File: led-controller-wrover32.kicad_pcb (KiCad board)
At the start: 4 copper layers, 36 x 40 mm, 130 parts, among them J101 Molex PicoBlade 6-pin, J102 Molex PicoBlade 4-pin, J103 STATUS OUT, J104 USB_B_Micro, J105 POWER IN, J106 Molex PicoBlade 6-pin, J107 5V_LOGIC, J201 12V_OUT, J301 Micro_SD_Card, J302 Molex PicoBlade 4-pin, J401 Fan PWM, J402 GPIO_CONN, Q101 UMH3N, Q102 BSS138, Q301 BSS138, Q401 SIL2301-TP, Q402 EM6K7T2R, SW301 KMR2, SW302 KMR2, U101 USBUF02W6, U102 ESP32-S3-WROOM-2-N32R8V, U103 NTS0104BQ,115, U104 TCA9406ZYPR, U201 TPS55340-Q1, U202 MPM3810GQB-33, U301 SSM2518CPZ, U401 BNO085, U402 PCA9575HF, Y401 OM-7604-C7

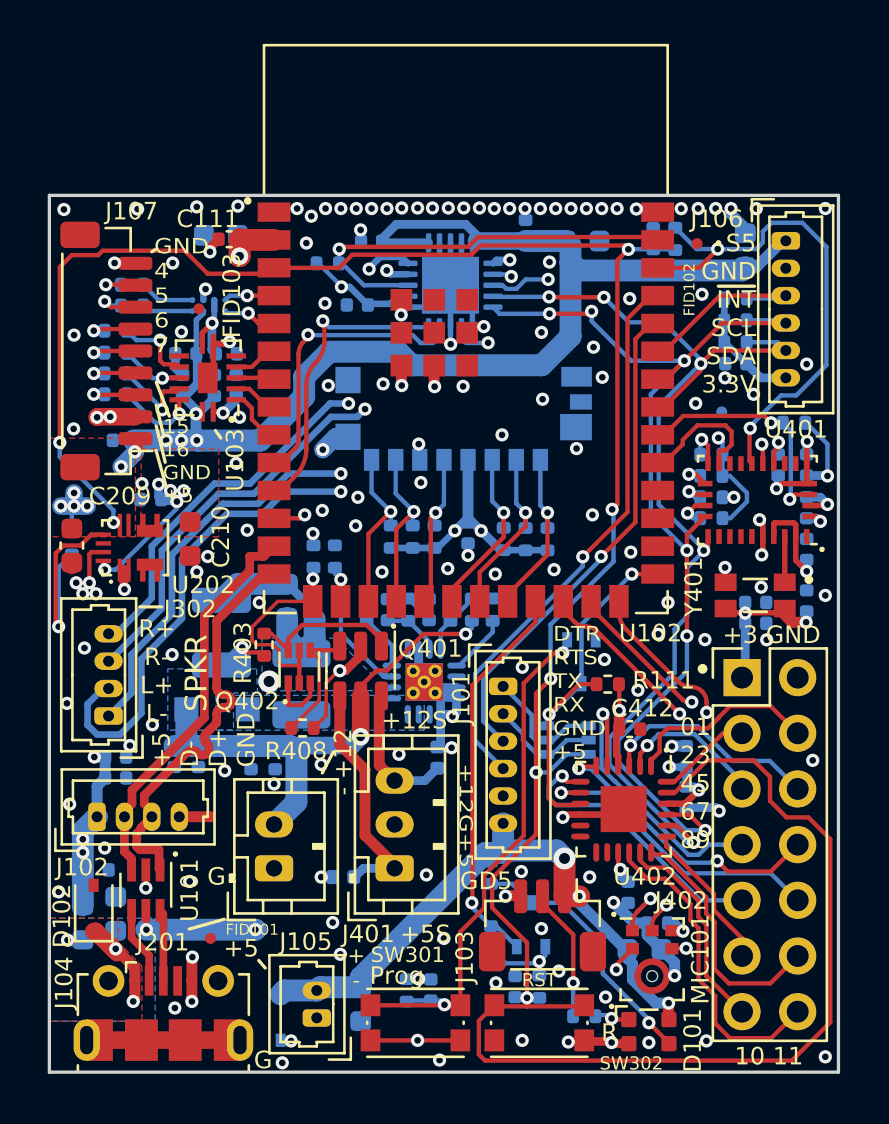
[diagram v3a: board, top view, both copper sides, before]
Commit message: Switched to a different 12V booster chip and increased 12V from 500ma to 1A.
Also:
- Switched most 10uF capacitors to 0402 footprints.
- Other cleanup

Signed-off-by: Aaron Williams <aaron.w2@gmail.com>
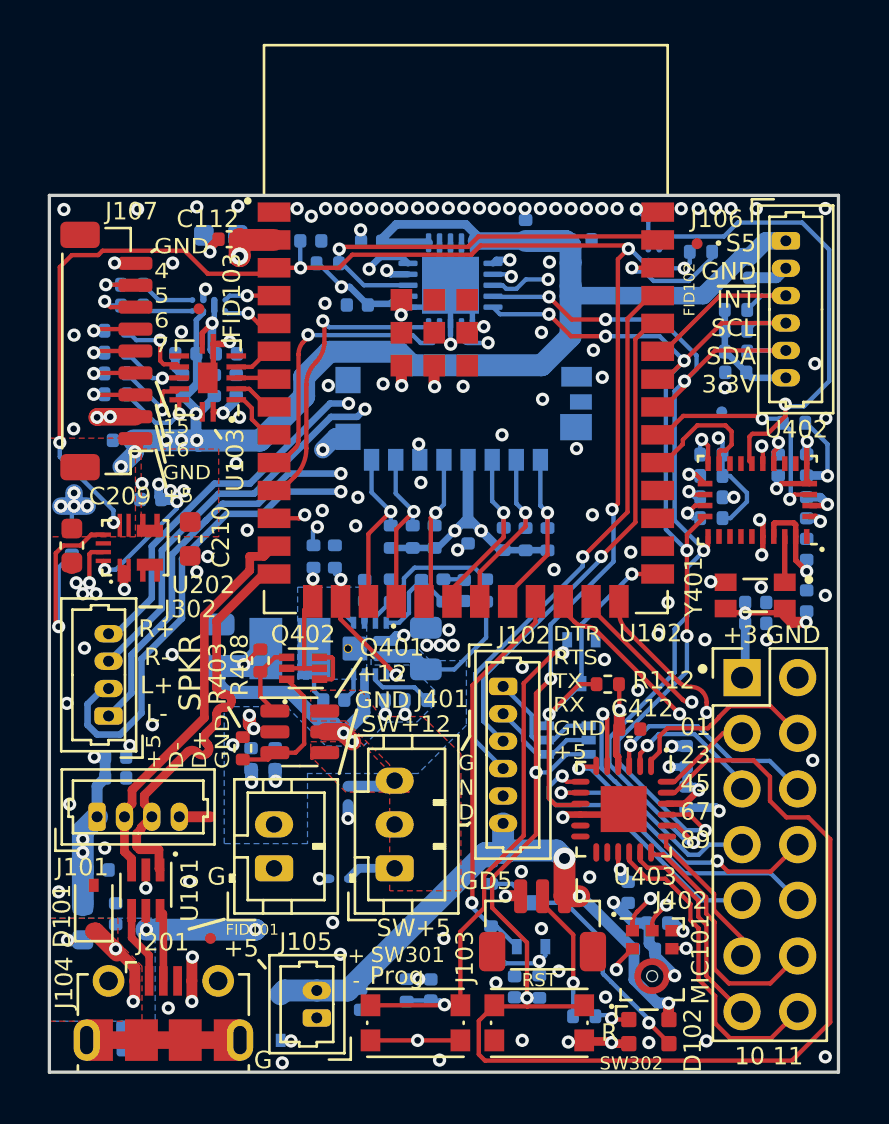
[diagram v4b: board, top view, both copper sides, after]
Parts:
- removed C201: 47uF, Capacitor_SMD:C_1210_3225Metric
- removed C202: 1uF, Capacitor_SMD:C_0402_1005Metric
- removed C203, C205: 0.1uF, Capacitor_SMD:C_0402_1005Metric
- removed C204: 22uF, Capacitor_SMD:C_0603_1608Metric
- removed C206: 22nF, Capacitor_SMD:C_0402_1005Metric
- removed C207: 1.5nF, Capacitor_SMD:C_0402_1005Metric
- removed C208: 33nF, Capacitor_SMD:C_0402_1005Metric
- removed D201: SMD34PL-TP, Diode_SMD:D_SOD-123F
- removed L201: 2.2uH, Inductor_SMD:L_1210_3225Metric
- removed R201: 86.6K, Resistor_SMD:R_0402_1005Metric
- removed R203: 18.7K, Resistor_SMD:R_0402_1005Metric
- removed R204: 10K, Resistor_SMD:R_0402_1005Metric
- removed R205: 1.54K, Resistor_SMD:R_0402_1005Metric
- removed U201: TPS55340-Q1, Aaron:QFN-16-1EP_3x3mm_P0.5mm_EP2.7x2.7mm_ThermalVias
- added C107: 0.47uF, Capacitor_SMD:C_0402_1005Metric, B.Cu at (63.8, 69.0)
- added C212: 47uF 10V, Capacitor_SMD:C_0805_2012Metric, B.Cu at (67.7, 50.5)
- added C213: 0.1uF, Capacitor_SMD:C_0402_1005Metric, B.Cu at (74.8, 53.0)
- added C214: 0.1uF, Capacitor_SMD:C_0402_1005Metric, B.Cu at (73.0, 53.0)
- added C215: 10uF 50V, Capacitor_SMD:C_0805_2012Metric, B.Cu at (77.2, 50.7)
- added C216: 10uF, Capacitor_SMD:C_0402_1005Metric, B.Cu at (74.4, 48.0)
- added C217: 150pF, Capacitor_SMD:C_0402_1005Metric, B.Cu at (78.9, 48.0)
- added C218: 10pF, Capacitor_SMD:C_0402_1005Metric, B.Cu at (77.0, 48.0)
- added L202: 0.47uH, Inductor_SMD:L_Bourns_SRP3212, B.Cu at (71.0, 50.7)
- added R104: 1M, Resistor_SMD:R_0402_1005Metric, B.Cu at (63.8, 68.0)
- added R207: 41.2K, Resistor_SMD:R_0402_1005Metric, B.Cu at (72.6, 48.3)
- added R208: 1M, Resistor_SMD:R_0402_1005Metric, B.Cu at (79.9, 48.0)
- added R209: 110K, Resistor_SMD:R_0402_1005Metric, B.Cu at (75.6, 48.0)
- added R210: 68.1K, Resistor_SMD:R_0402_1005Metric, B.Cu at (78.0, 48.0)
- added R211: 205K, Resistor_SMD:R_0402_1005Metric, B.Cu at (76.7, 53.0)
- added U203: TPS61089RNRR, Package_DFN_QFN:Texas_S_VQFN-11_2.0x2.5mm_P0.5mm_Thermal, B.Cu at (74.6, 50.7)
- added U401: SN74AUP1G08YZP, Package_BGA:Texas_DSBGA-5_0.9x1.4mm_Layout2x1x2_P0.5mm, B.Cu at (87.6, 33.0)
- C102, C103, C106, C306: footprint Capacitor_SMD:C_0603_1608Metric -> Capacitor_SMD:C_0402_1005Metric
- C113: renamed from C112; footprint Capacitor_SMD:C_0603_1608Metric -> Capacitor_SMD:C_0402_1005Metric
- D401, D402: value CDBQR0230R-HF -> NSR05T40P2T5G; footprint Diode_SMD:D_0402_1005Metric -> Diode_SMD:D_SOD-923
- moved C304 35.3 mm to (71.9, 32.1), turned to 0 degrees
- moved C303 34.7 mm to (81.2, 66.1)
- moved R403 4.82 mm to (68.8, 55.2), turned to -90 degrees
- moved D401 4.43 mm to (73.6, 57.4), turned to -90 degrees
- moved Q401 3.92 mm to (71.4, 54.5), turned to 0 degrees
- moved R408 3.63 mm to (69.6, 51.2), turned to -90 degrees
- moved R401 1.31 mm to (89.7, 32.6), turned to 0 degrees
- moved C113 0.80 mm to (92.0, 33.3), turned to -90 degrees
- moved R109 0.53 mm to (91.3, 35.2)
- moved R110 0.48 mm to (91.3, 36.2)
- moved R111 0.43 mm to (91.3, 37.1)
- moved C114 0.40 mm to (91.3, 38.1)
- moved C106 0.23 mm to (74.2, 66.7)
- moved D402 0.19 mm to (73.2, 61.2)
- moved Q402 0.19 mm to (71.6, 51.6), turned to 180 degrees
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- renumbered C107 to C108, C108 to C109, C109 to C110, C110 to C111, C111 to C112, C113 to C114, C114 to C115, C115 to C116, C116 to C117, C117 to C118, C304 to C303, C303 to C304, D102 to D101, D101 to D102, J102 to J101, J101 to J102, R104 to R105, R105 to R106, R106 to R107, R107 to R108, R108 to R109, R109 to R110, R110 to R111, R111 to R112, R112 to R113, R113 to R114, U401 to U402, U402 to U403
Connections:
- J104 pad 6: unconnected-(J104-Pad6) -> Net-(C107-Pad1)
- Q401 pad 1: /Motion and GPIO/~{EN_12V} -> /Motion and GPIO/~{EN_5V}
- Q401 pad 2: +5V -> +12V
- Q401 pad 3: /Motion and GPIO/~{EN_5V} -> /Motion and GPIO/~{EN_12V}
- Q401 pad 4: /Motion and GPIO/SW_5V_IO1 -> /Motion and GPIO/SW_12V
- Q401 pad 5: +12V -> +5V
- Q401 pad 6: /Motion and GPIO/SW_12V -> /Motion and GPIO/SW_5V_IO1
- R401 pad 1: ~{RESET} -> +3V3
- U402 pad 11: ~{RST_BNO085} -> Net-(U401-PadC2)
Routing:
- net Net-(U401-PadC2): track 0.00 -> 21.1 mm, vias 0 -> 1
- net ~{RST_BNO085}: track 23.4 -> 5.90 mm, vias 2 -> 1
- net +12V: track 25.1 -> 7.77 mm
- net Net-(C107-Pad1): track 0.00 -> 15.8 mm
- net unconnected-(J104-Pad6): track 13.2 -> 0.00 mm
- net GND: track 70.3 -> 59.9 mm, vias 155 -> 150
- net /Motion and GPIO/SW_5V_IO1: track 10.7 -> 2.30 mm
- net +5V: track 105.6 -> 114.0 mm, vias 18 -> 19
- net /Motion and GPIO/SW_12V: track 6.38 -> 1.87 mm
- net /Power Supplies/FB: track 2.88 -> 6.60 mm
- net FAN_PWM: track 9.89 -> 6.28 mm
- net /Power Supplies/ILIM: track 0.00 -> 3.00 mm
- net /Power Supplies/FREQ: track 2.67 -> 0.00 mm
- net /Power Supplies/SS: track 2.55 -> 0.00 mm
- net /Power Supplies/SW: track 0.00 -> 2.52 mm
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- added copper zone on F.Cu, net /Motion and GPIO/SW_12V
- added copper zone on F.Cu, net /Motion and GPIO/SW_5V_IO1
- removed copper zone on B.Cu, net +5V
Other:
- board text added: "+12 GND"
- board text added: "G N D"
- board text added: "GND SW5"
- board text added: "SW+12"
- board text added: "SW+5"
- board text removed: "+12 GND +5"
- board text removed: "+12G+5"
- board text removed: "+12S"
- board text removed: "+5S"
- board text removed: "- +12"

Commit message: Latest 4.0 settings for pcbway
Signed-off-by: Aaron Williams <aaron.w2@gmail.com>
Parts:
- removed the C102 at (87.2, 64.4)
- removed the C103 at (63.0, 62.8)
- removed the C116 at (66.2, 37.2)
- removed Q102: BSS138, Package_TO_SOT_SMD:SOT-323_SC-70
- removed the R101 at (80.2, 63.9)
- removed the R102 at (80.2, 60.9)
- removed R113, R114: 33, Resistor_SMD:R_0402_1005Metric
- removed the R202 at (73.0, 46.5)
- removed the R405 at (90.2, 42.8)
- removed the U104 at (67.3, 35.0)
- removed the U403 at (86.2, 58.0)
- added C101: 1uF, Capacitor_SMD:C_0402_1005Metric, B.Cu at (87.1, 64.5)
- added C115: 1uF, Capacitor_SMD:C_0402_1005Metric, B.Cu at (69.8, 33.4)
- added C404: 0.1uF, Capacitor_SMD:C_0402_1005Metric, B.Cu at (87.3, 41.3)
- added C405: 0.1uF, Capacitor_SMD:C_0402_1005Metric, B.Cu at (87.0, 45.2)
- added C410: 1uF, Capacitor_SMD:C_0402_1005Metric, B.Cu at (77.7, 57.4)
- added C415: 1uF, Capacitor_SMD:C_0402_1005Metric, B.Cu at (77.7, 59.3)
- added JP101: IO4_IN_FILT, Jumper:SolderJumper-2_P1.3mm_Open_RoundedPad1.0x1.5mm, B.Cu at (69.3, 35.5)
- added R107: 10K, Resistor_SMD:R_0402_1005Metric, B.Cu at (73.0, 46.5)
- added R403: 2.2K, Resistor_SMD:R_0402_1005Metric, B.Cu at (90.2, 41.8)
- added TP101: TP +5_filtered, TestPoint:TestPoint_Pad_1.0x1.0mm, B.Cu at (61.0, 55.9)
- added TP102: TP +5_USB, TestPoint:TestPoint_Pad_1.0x1.0mm, B.Cu at (60.9, 66.6)
- added TP301: ~{RESET}, TestPoint:TestPoint_Pad_1.0x1.0mm, B.Cu at (61.0, 34.5)
- added U101: TPS2001DDBVX, Package_TO_SOT_SMD:SOT-23-5, B.Cu at (63.9, 61.5)
- added U402: BME280, Package_LGA:Bosch_LGA-8_2.5x2.5mm_P0.65mm_ClockwisePinNumbering, B.Cu at (87.5, 43.2)
- added U404: SX1509BIULTRT, Aaron:QFN-28-1EP_4x4mm_P0.4mm_EP2.65x2.65mm, F.Cu at (85.9, 57.9)
- C102: renamed from C104; value 0.1uF -> 1uF
- D101: value UDD32C12L01 -> TPD1E10B06DPYR; footprint Diode_SMD:D_SOD-323 -> Diode_SMD:D_0402_1005Metric
- D102: footprint marbastlib-various:LED_WS2812_2020 -> Aaron:LED_WS2812_2020
- R108: renamed from R109; value 4.7K -> 10K
- R404: value 4.7K -> 2.2K
- R407: renamed from R403; value 10K -> 110K
- R409: renamed from R408; value 10K -> 110K
- U103: renamed from U102; value ESP32-S3-WROOM-2-N32R8V -> ESP32-S3-WROOM-2-N32R8; footprint Aaron:ESP32-S3-WROOM-2-N32R8V -> Espressif:ESP32-S3-WROOM-2
- moved C413 7.55 mm to (82.5, 59.4), turned to 180 degrees
- moved C414 6.62 mm to (82.5, 58.4), turned to 180 degrees
- moved C103 6.22 mm to (66.9, 60.5)
- moved C114 5.62 mm to (64.2, 33.1)
- moved U103 2.95 mm to (79.0, 39.0)
- moved C102 1.43 mm to (60.8, 60.5), turned to 90 degrees
- moved R404 0.97 mm to (90.2, 42.8)
- moved R206 0.74 mm to (61.7, 45.5)
- moved J402 0.64 mm to (91.7, 51.4)
- moved C416 0.60 mm to (92.2, 48.0)
- moved C412 0.55 mm to (85.8, 61.9)
- moved C417 0.55 mm to (92.2, 49.0)
- moved FB101 0.50 mm to (61.1, 62.9)
- moved D101 0.41 mm to (62.2, 62.9)
- moved C107 0.40 mm to (68.1, 38.7)
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- renumbered C101 to C103, C105 to C104, C106 to C105, C107 to C106, C108 to C107, C109 to C108, C110 to C109, C111 to C110, C112 to C111, C113 to C112, C114 to C113, C115 to C114, C117 to C116, C118 to C117, C212 to C201, C214 to C202, C215 to C203, C213 to C204, C216 to C205, C217 to C206, C218 to C207, C209 to C208, C210 to C209, C211 to C210, C404 to C406, C405 to C408, C406 to C409, C412 to C411, C413 to C412, C410 to C413, C411 to C414, C408 to C416, C409 to C417, L202 to L201, R103 to R101, R104 to R102, R105 to R103, R106 to R104, R107 to R105, R108 to R106, R110 to R109, R111 to R110, R112 to R111, R207 to R201, R208 to R202, R210 to R203, R209 to R204, R211 to R205, R407 to R405, R409 to R406, R406 to R408, U101 to U102, U103 to U104, U203 to U201, U402 to U403
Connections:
- net /Motion and GPIO/SW_5V_IO1 renamed /Motion and GPIO/SW_5V
- net Net-(U401-PadC2) renamed /Motion and GPIO/~{BNO085_RST}
- C102 pad 1: +5V -> /FVUSB
- D102 pad 3: /STS_5V -> /STATUS_LED
- FB101 pad 2: +5V -> /FVUSB
- J107 pad 7: /IO5_H -> /IO5
- J107 pad 8: /IO4_H -> /IO4
- J107 pad 9: GND -> +3V3
- J402 pad 11: /Motion and GPIO/P1_0 -> /Motion and GPIO/P0_14
- J402 pad 12: /Motion and GPIO/P1_1 -> /Motion and GPIO/P0_15
- J402 pad 13: /Motion and GPIO/P1_2 -> /Motion and GPIO/P0_12
- J402 pad 14: /Motion and GPIO/P1_3 -> /Motion and GPIO/P0_13
- J402 pad 3: /Motion and GPIO/P0_0 -> /Motion and GPIO/P0_2
- J402 pad 4: /Motion and GPIO/P0_1 -> /Motion and GPIO/P0_3
- J402 pad 5: /Motion and GPIO/P0_2 -> /Motion and GPIO/P0_0
- J402 pad 6: /Motion and GPIO/P0_3 -> /Motion and GPIO/P0_1
- R404 pad 1: /Motion and GPIO/H_SCL -> /Motion and GPIO/S_SDA
- U301 pad 3: +3V3 -> GND
- U403 pad 15: /Motion and GPIO/H_SCL -> /Motion and GPIO/S_SCL
- U403 pad 16: /Motion and GPIO/H_SDA -> /Motion and GPIO/S_SDA
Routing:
- net /Motion and GPIO/P1_3: track 14.5 -> 0.00 mm
- net +5V: track 114.0 -> 101.5 mm, vias 19 -> 22
- net /Motion and GPIO/P0_13: track 0.00 -> 12.1 mm
- net /STS_5V: track 12.1 -> 0.00 mm, vias 1 -> 0
- net /Motion and GPIO/P1_1: track 11.3 -> 0.00 mm
- net /Motion and GPIO/P0_12: track 0.00 -> 10.3 mm
- net GND: track 59.9 -> 69.8 mm, vias 150 -> 183
- net /Motion and GPIO/P1_2: track 9.71 -> 0.00 mm
- net /Motion and GPIO/P0_15: track 0.00 -> 9.11 mm
- net /STATUS_LED: track 17.6 -> 26.3 mm, vias 1 -> 2
- net /Motion and GPIO/P0_14: track 0.00 -> 7.24 mm
- net /Motion and GPIO/P1_0: track 6.16 -> 0.00 mm
- net /IO4: track 2.31 -> 7.19 mm
- net /IO5: track 2.46 -> 6.80 mm, vias 1 -> 0
- net +3V3: track 90.9 -> 94.3 mm, vias 31 -> 33
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- added copper zone on B.Cu, net +5V
- added copper zone on B.Cu, net /FVUSB
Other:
- board text added: "+3 4 5 6 7"
- board text added: "DT RTS TX RX GN +5"
- board text added: "GND"
- board text added: "GND SW 5"
- board text added: "JP101 filter IO4"
- board text added: "SW 12"
- board text added: "~{RESET}"
- board text removed: "+3 GND"
- board text removed: "D R TX RX GND +5V"
- board text removed: "GND 4 5 6 7"
- board text removed: "GND SW5"
